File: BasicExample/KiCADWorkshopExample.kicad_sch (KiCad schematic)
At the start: 21 parts, among them P1 USB_C_Plug_USB2.0, SW1 SW_Push, SW2 SW_Push, SW3 SW_Push, SW4 SW_Push, U1 BD30FC0WFP

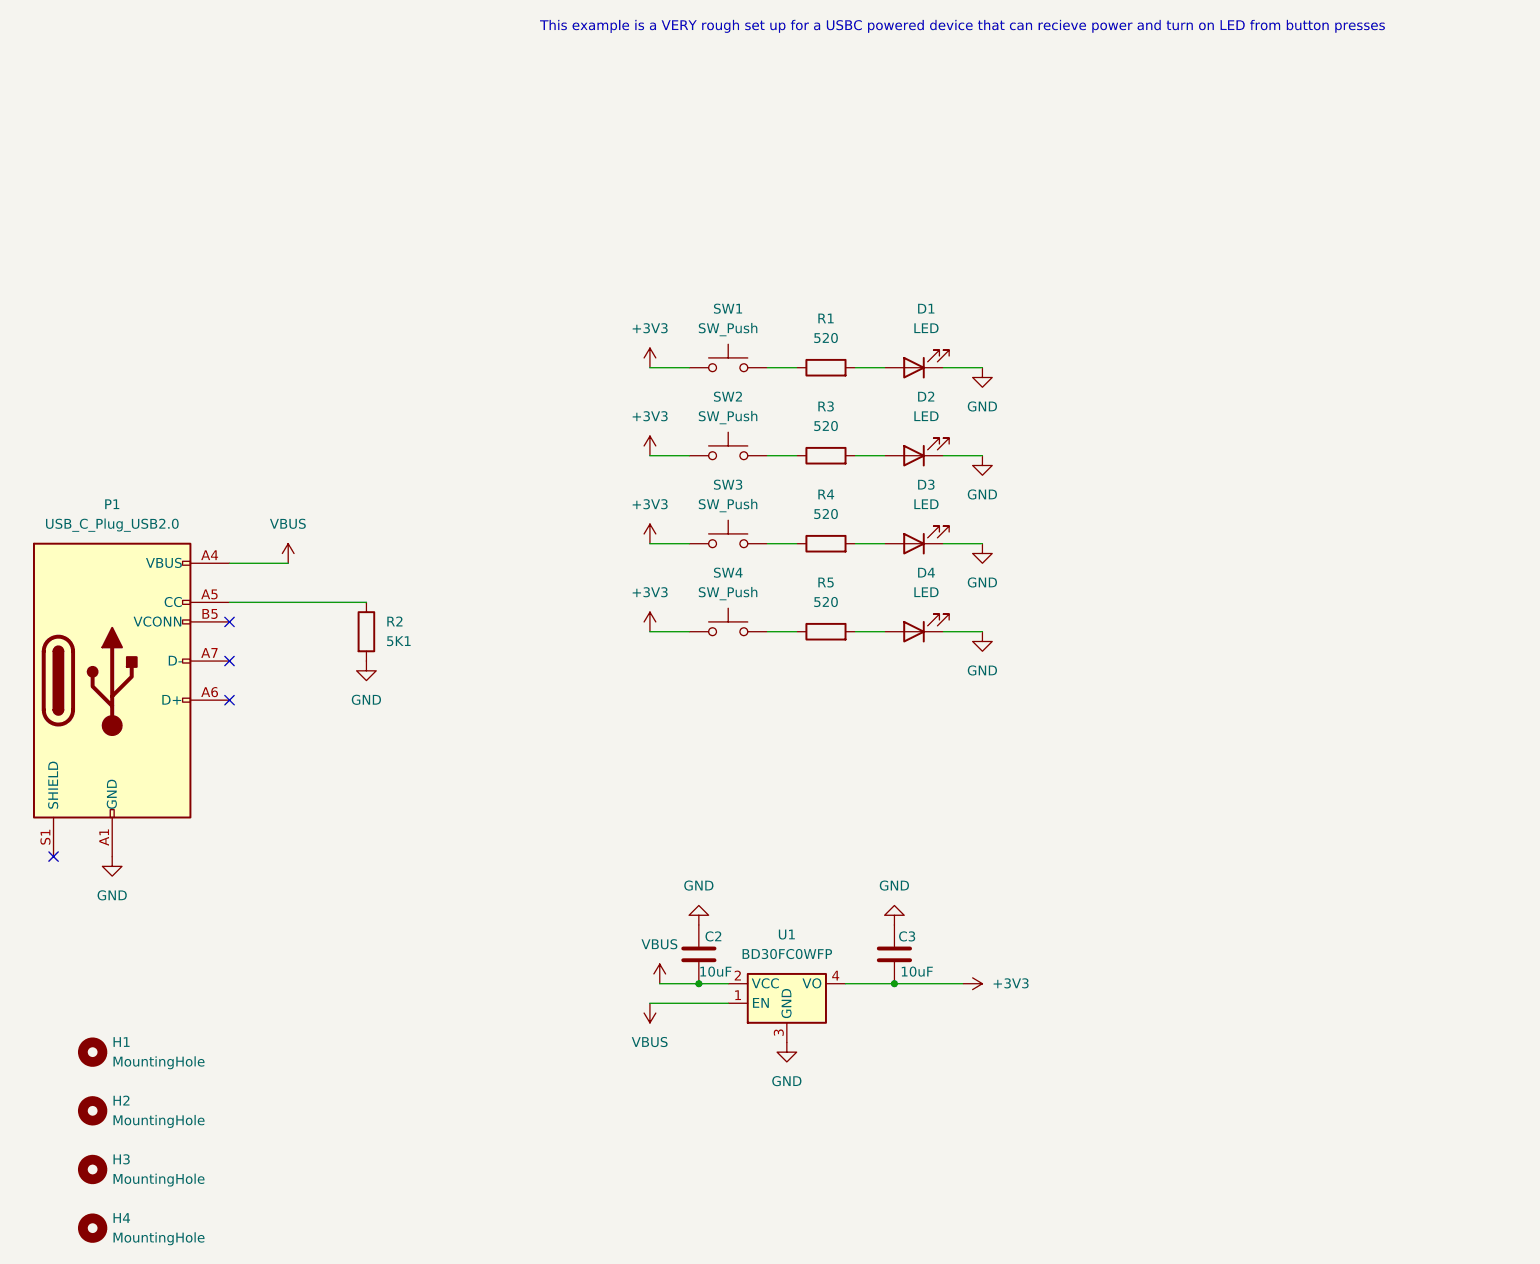
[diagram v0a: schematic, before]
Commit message: complete simple tut
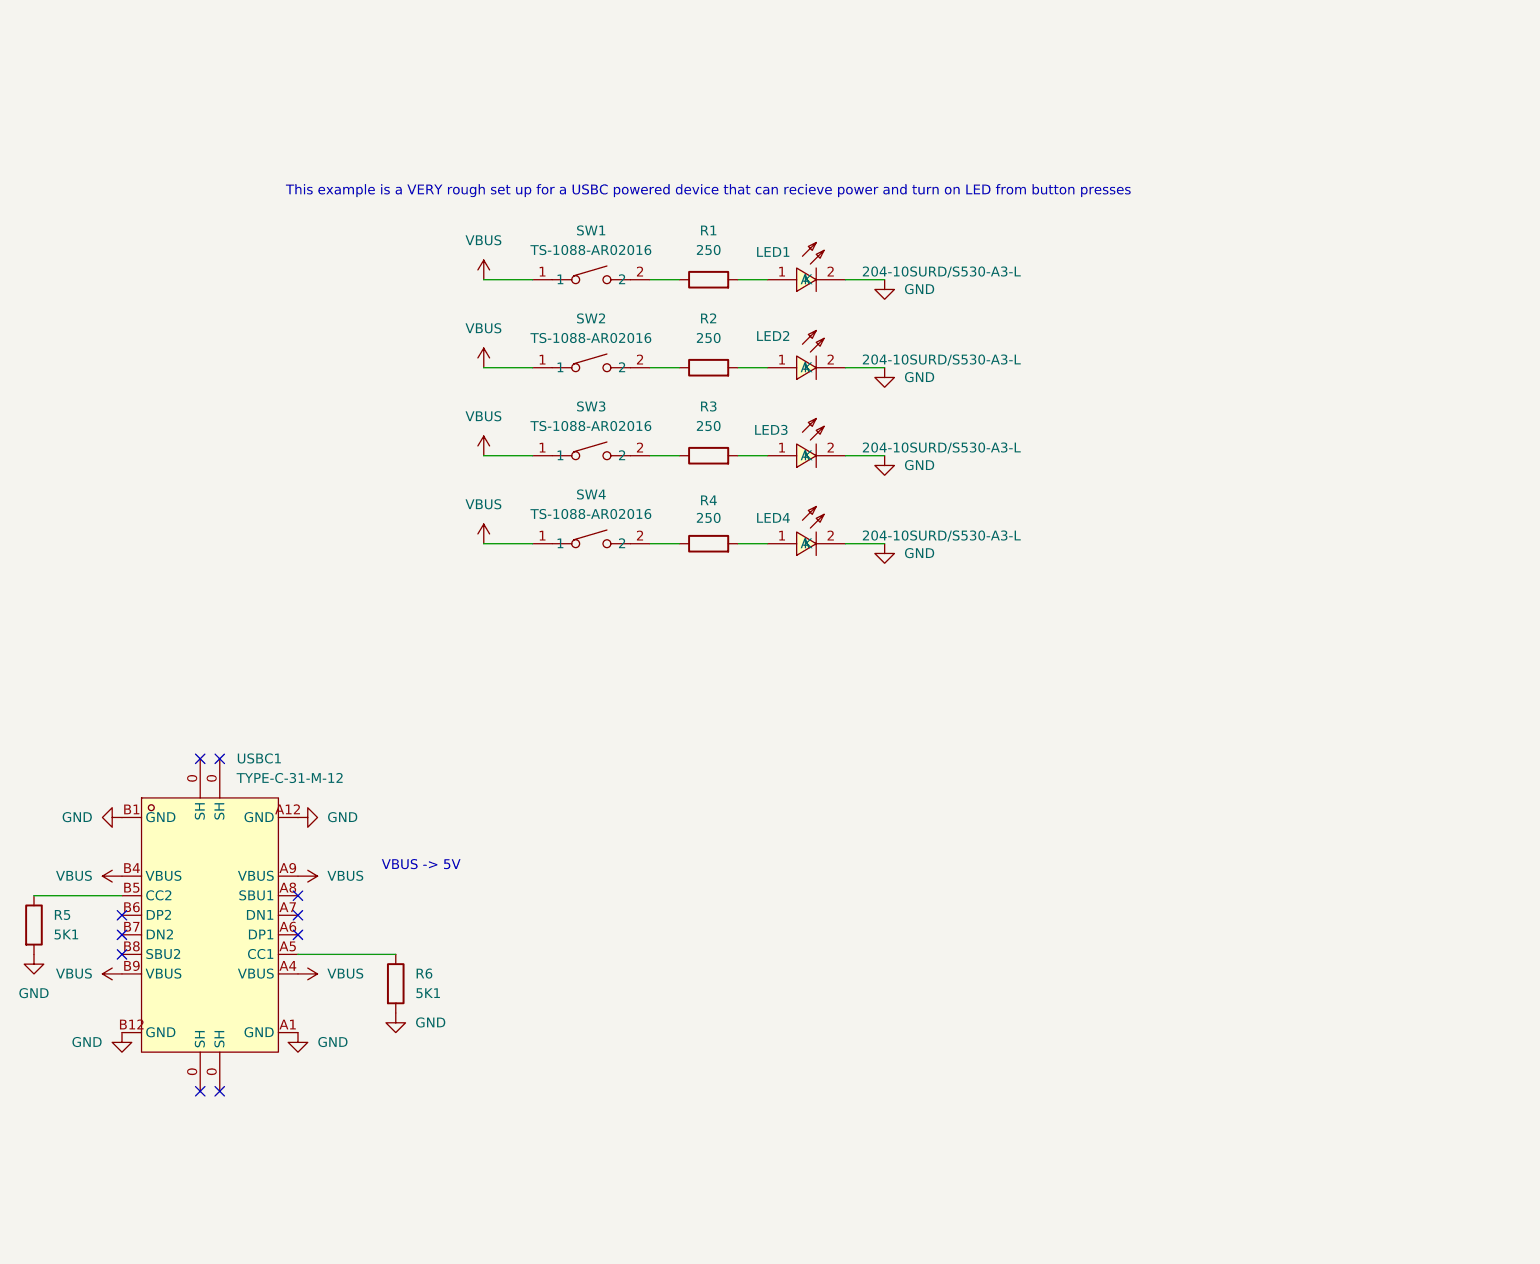
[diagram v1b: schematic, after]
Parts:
- removed C2, C3: 10uF, Capacitor_SMD:C_0603_1608Metric, symbol Device:C
- removed D1, D2, D3, D4: LED, LED_SMD:LED_2010_5025Metric, symbol Device:LED
- removed H1, H2, H3, H4: MountingHole, MountingHole:MountingHole_4mm, symbol Mechanical:MountingHole
- removed P1: USB_C_Plug_USB2.0, Connector_USB:USB_C_Plug_ShenzhenJingTuoJin_918-118A2021Y40002_Vertical, symbol Connector:USB_C_Plug_USB2.0
- removed SW1, SW2, SW3, SW4: SW_Push, Button_Switch_THT:SW_CW_GPTS203211B, symbol Switch:SW_Push
- removed U1: BD30FC0WFP, Package_TO_SOT_SMD:TO-252-4, symbol Regulator_Linear:BD30FC0WFP
- added LED1, LED2, LED3, LED4: 204-10SURD/S530-A3-L, red:LED-TH_BD3.0-P2.54-FD, symbol red:204-10SURD_S530-A3-L
- added R2: 250, Resistor_SMD:R_0805_2012Metric, symbol Device:R
- added SW1, SW2, SW3, SW4: TS-1088-AR02016, ts-1088:SW-SMD_L3.9-W3.0-P4.45, symbol ts-1088:TS-1088-AR02016
- added USBC1: TYPE-C-31-M-12, usbc:USB-C_SMD-TYPE-C-31-M-12, symbol usbc:TYPE-C-31-M-12
- R1, R3, R4: value 520 -> 250
- R5: value 520 -> 5K1; footprint Resistor_SMD:R_0805_2012Metric -> Resistor_SMD:R_0603_1608Metric
- renumbered R2 to R6
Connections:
- net GND: now also R5.2, LED1.2 (K), LED2.2 (K), LED3.2 (K), LED4.2 (K), USBC1.A1 (GND), USBC1.A12 (GND), USBC1.B1 (GND), USBC1.B12 (GND)
- net VBUS: now also SW1.1, SW2.1, SW3.1, SW4.1, USBC1.A4 (VBUS), USBC1.A9 (VBUS), USBC1.B4 (VBUS), USBC1.B9 (VBUS)
- net at R4.2: now also LED4.1 (A)
- net at R3.2: now also LED3.1 (A)
- net at R5.1: now also USBC1.B5 (CC2)
- net at R1.2: now also LED1.1 (A)
- net at R4.1: now also SW4.2
- net at R6.1: now also USBC1.A5 (CC1)
- net at R3.1: now also SW3.2
- net at R1.1: now also SW1.2
- new net: R2.1, SW2.2
- new net: LED2.1 (A), R2.2
- no-connect marks 4 -> 10
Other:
- note added: "VBUS -> 5V"
- moved on the sheet: R1, R6
